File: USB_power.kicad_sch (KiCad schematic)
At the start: 21 parts, among them J1 JST-4-pin, J1 TYPE-C-31-M12_13, U1 BQ24074RGTR, U4 TPD4E05U06DQAR

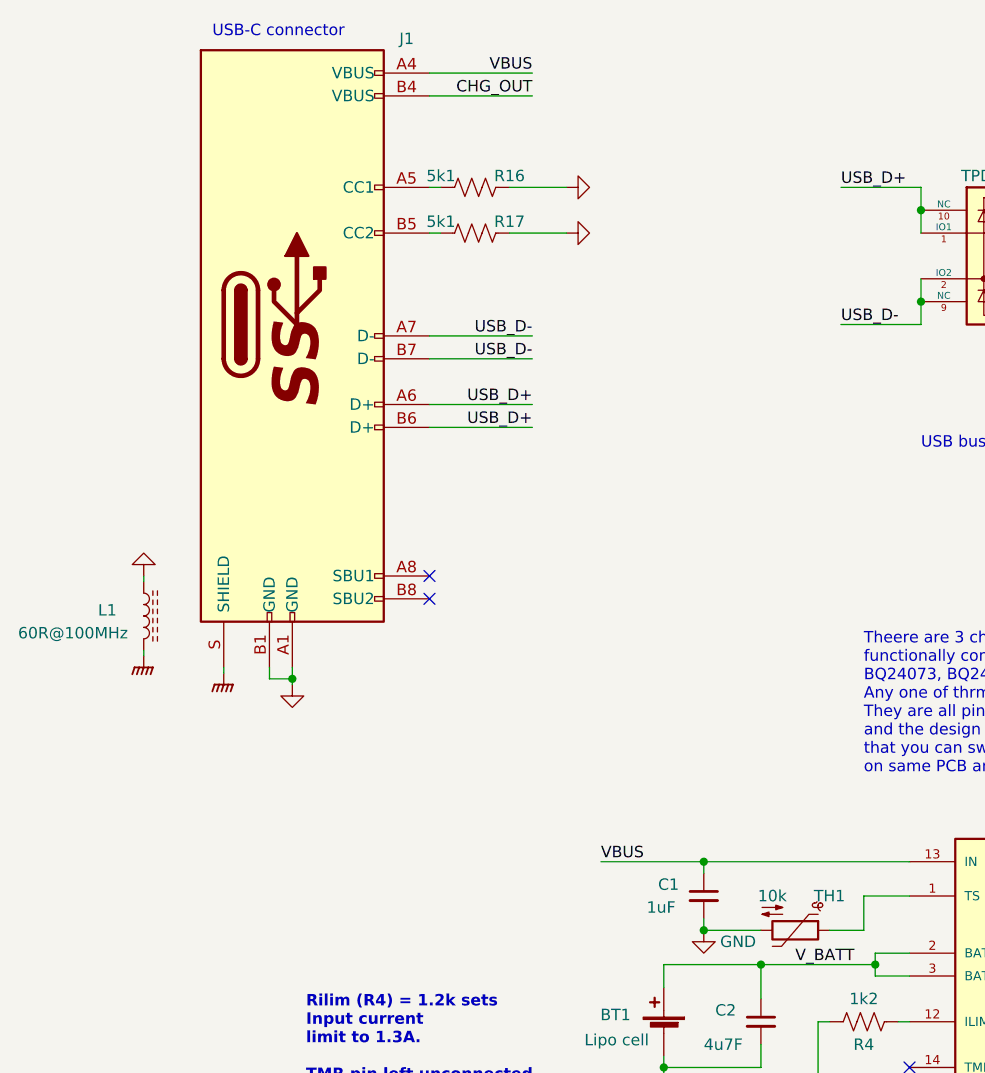
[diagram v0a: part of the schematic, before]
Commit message: RGB and Keys added to sch
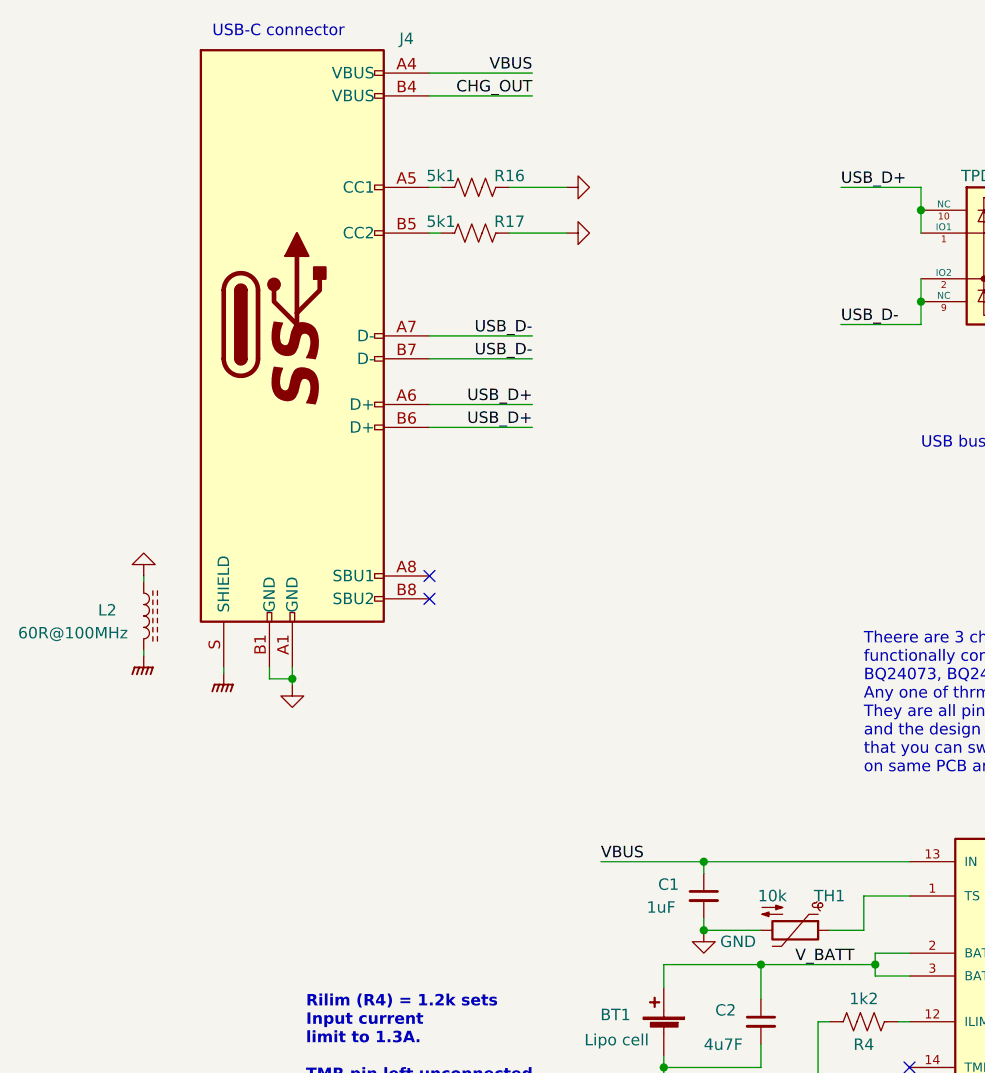
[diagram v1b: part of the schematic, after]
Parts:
- renumbered J1 to J4, L1 to L2

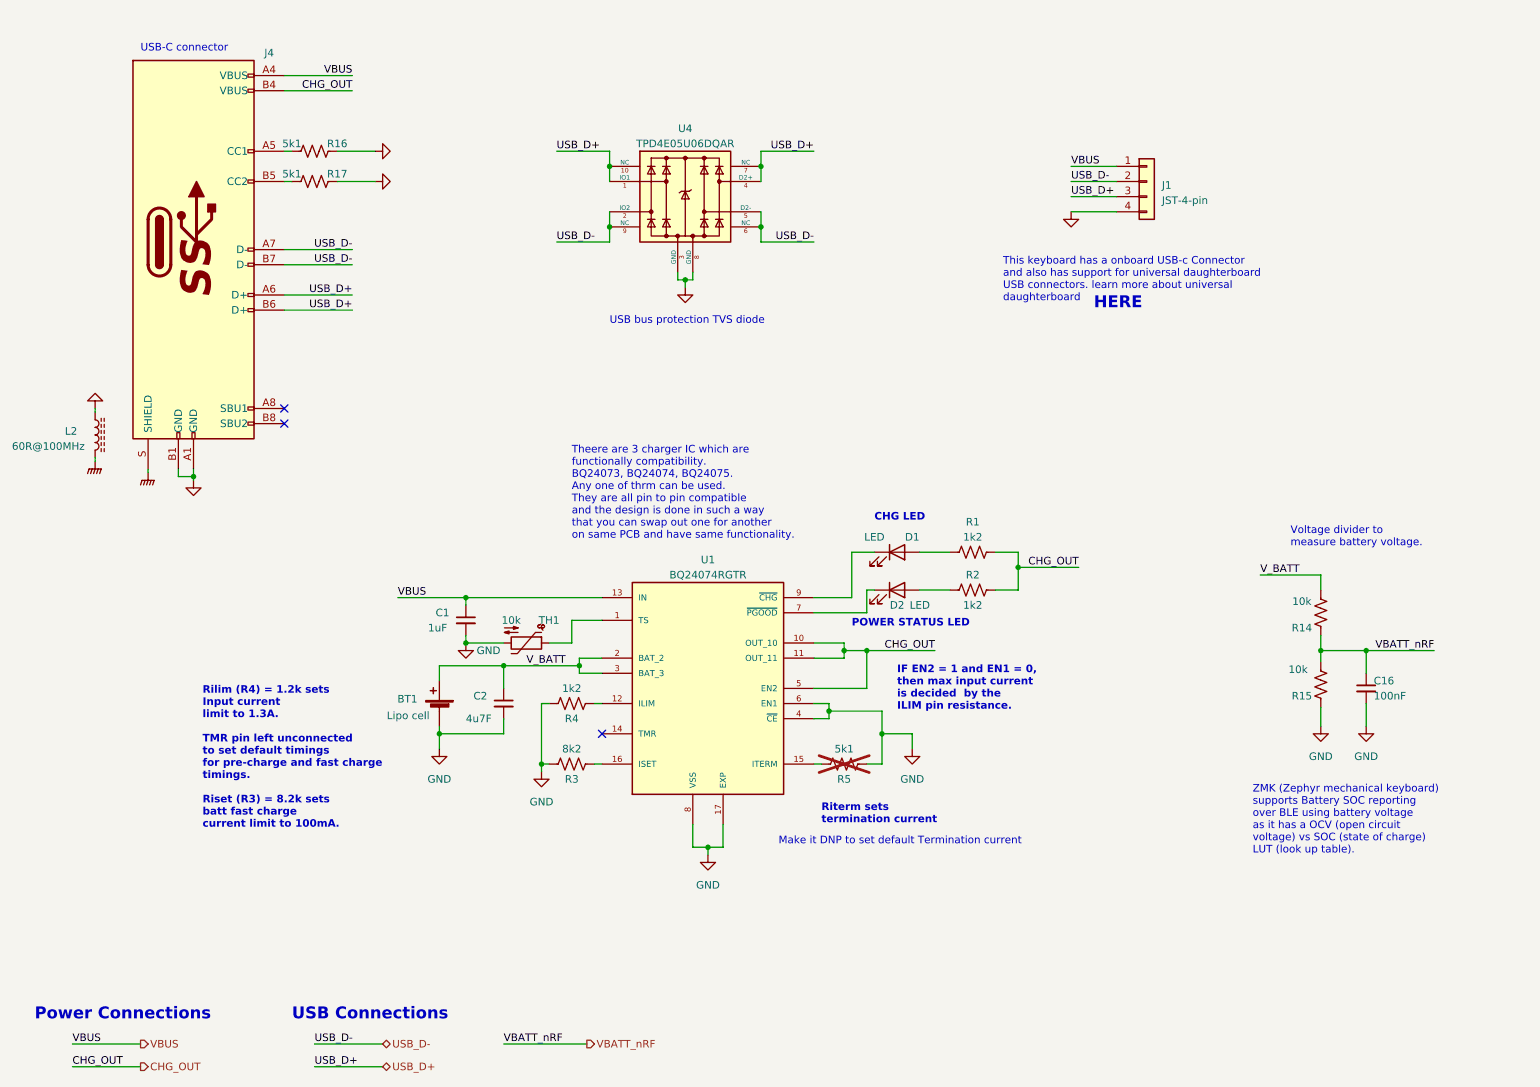
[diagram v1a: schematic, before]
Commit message: Layout start. Add symbols to proj lib
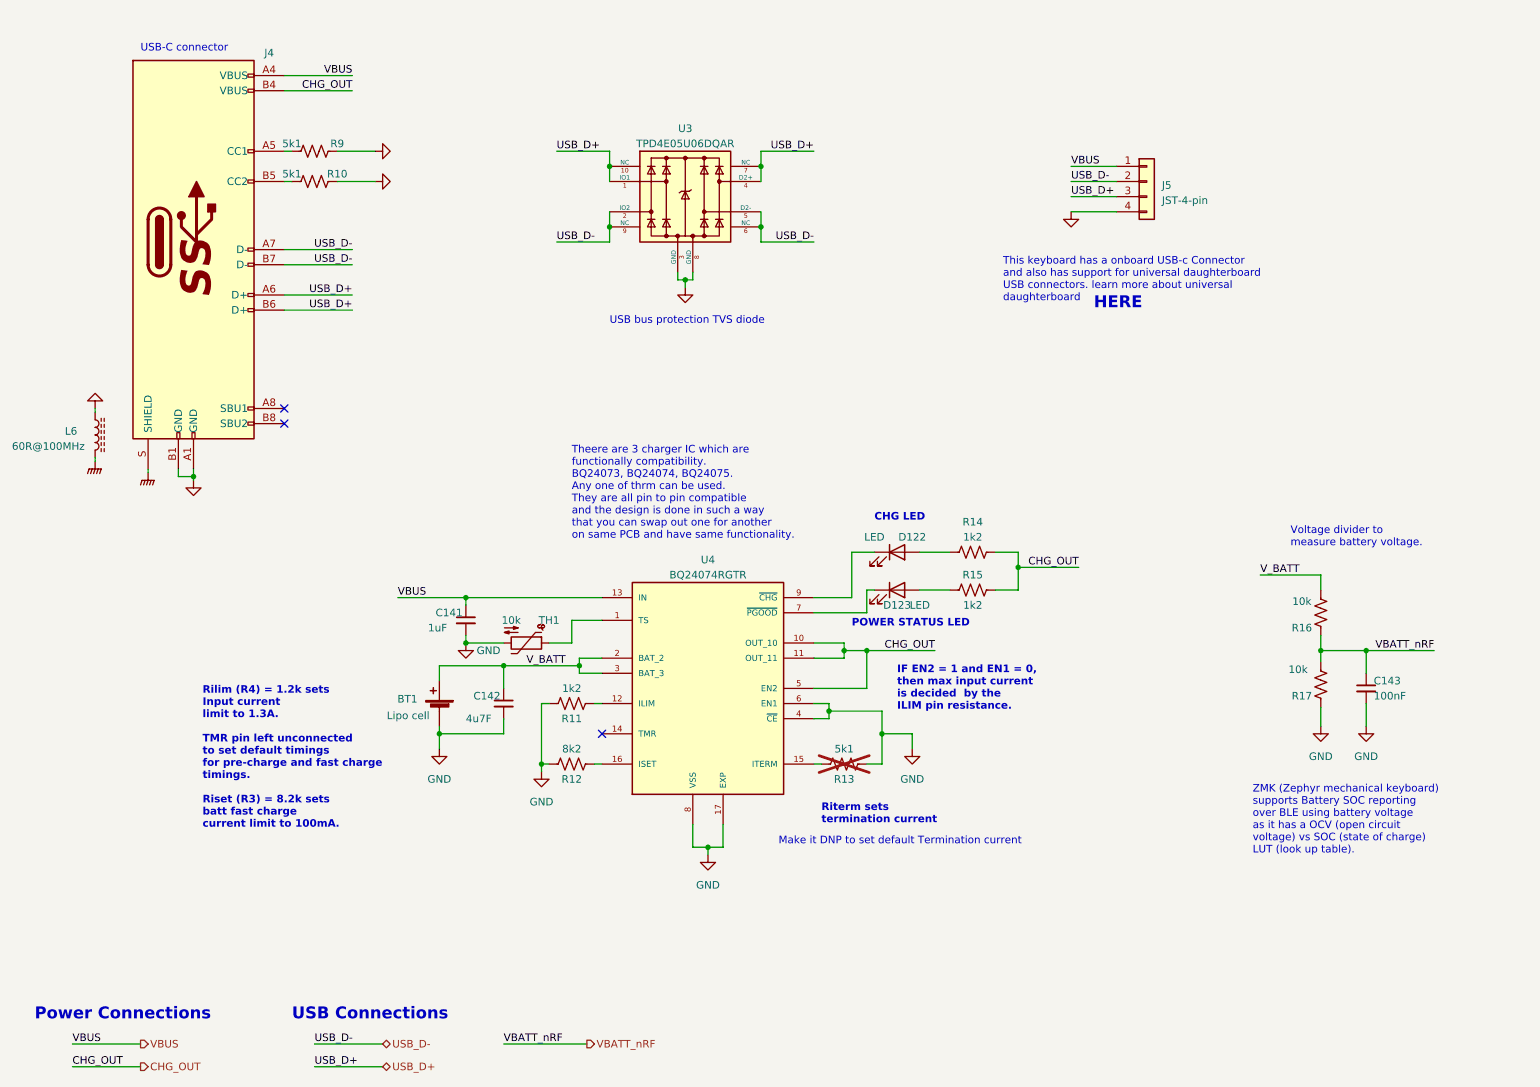
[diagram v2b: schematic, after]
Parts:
- renumbered C1 to C141, C2 to C142, C16 to C143, D1 to D122, D2 to D123, J1 to J5, L2 to L6, R17 to R10, R4 to R11, R3 to R12, R5 to R13, R1 to R14, R2 to R15, R14 to R16, R15 to R17, R16 to R9, U4 to U3, U1 to U4

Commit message: Status LEDs
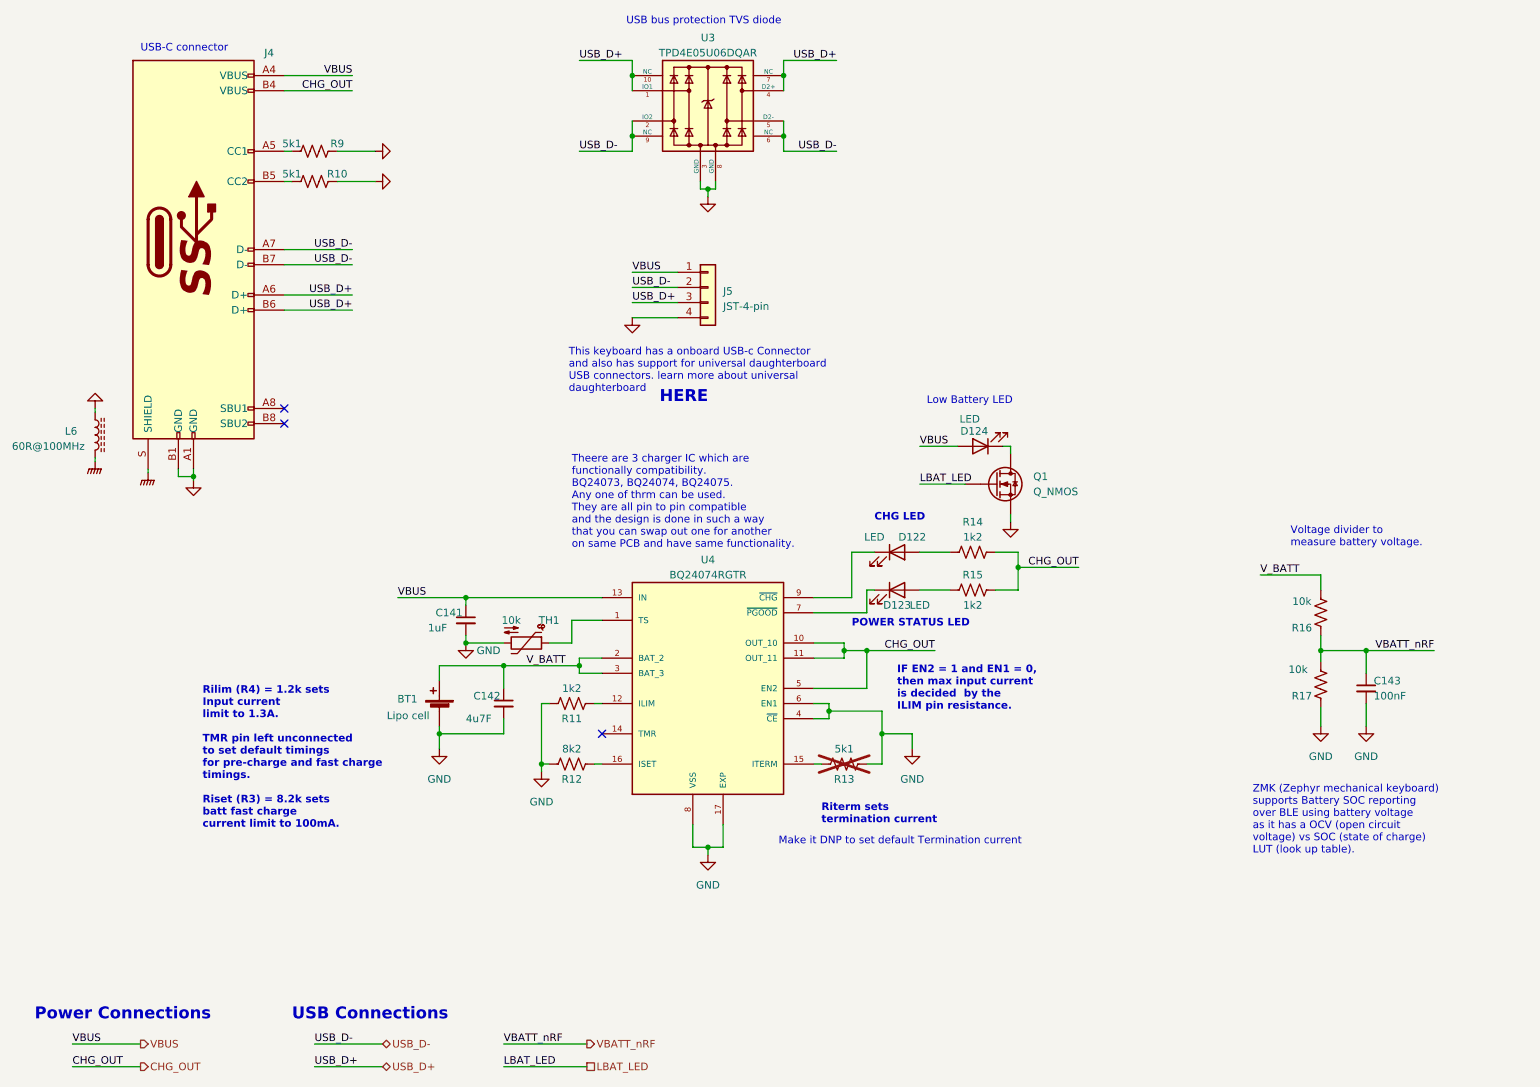
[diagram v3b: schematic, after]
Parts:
- added D124: LED, keyboard:LED_0603_1608Metric, symbol Device:LED
- added Q1: Q_NMOS, keyboard:SOT-23-3, symbol Device:Q_NMOS
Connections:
- net GND: now also Q1.S
- net VBUS: now also D124.2 (A)
- new net: D124.1 (K), Q1.D
- new net LBAT_LED: Q1.G
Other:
- note added: "Low Battery LED"
- moved on the sheet: J5, U3

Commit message: Status LED work
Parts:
- removed D123: LED, keyboard:LED_0603_1608Metric, symbol keyboard:LED
- added R19, R21: R_US, keyboard:R_0402_1005Metric, symbol keyboard:R_US
- R14, R15: value 1k2 -> R_US
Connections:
- net CHG_OUT: no longer R15.1
- net GND: now also R15.2
- net LBAT_LED: now also R21.1; no longer Q1.G
- net VBUS: now also R19.2; no longer D124.2 (A)
- new net: Q1.G, R15.1, R21.2
- new net: D124.2 (A), R19.1
- no-connect marks 3 -> 4
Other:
- note removed: "POWER STATUS LED"
- moved on the sheet: BT1, D122, D124, Q1

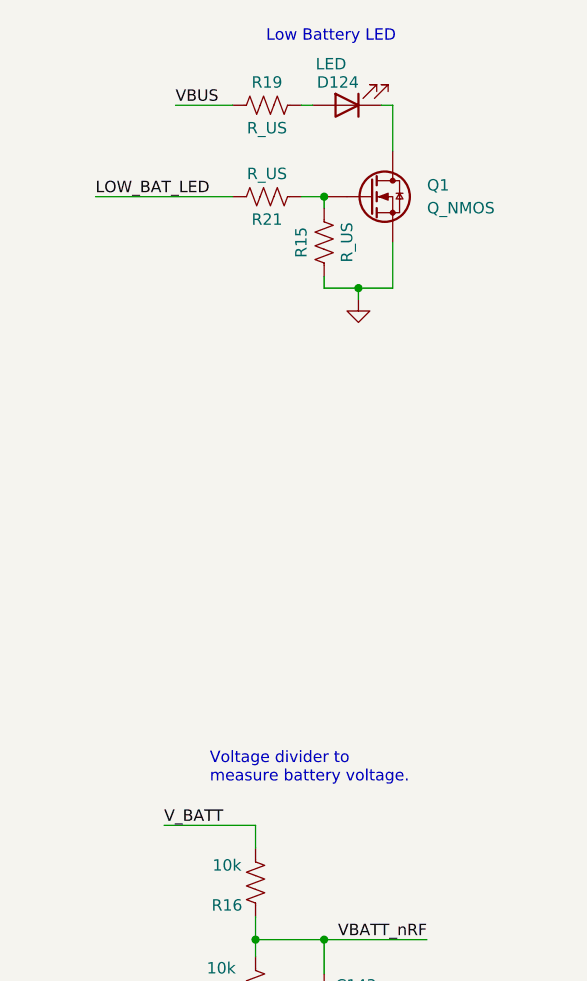
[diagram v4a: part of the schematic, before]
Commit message: Minor sch changes. Work towards matching g915 pcb dimensions
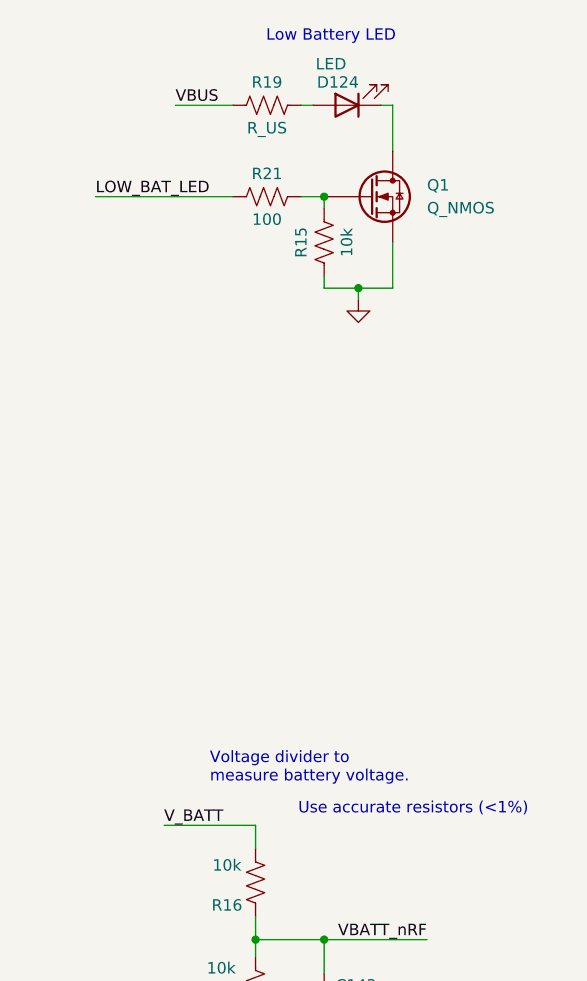
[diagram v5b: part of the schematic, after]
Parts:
- R15: value R_US -> 10k
- R21: value R_US -> 100
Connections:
- net LBAT_LED: now also R21.2; no longer R21.1
- net at Q1.G, R15.1: now also R21.1; no longer R21.2
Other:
- note added: "Use accurate resistors (<1%)"
- moved on the sheet: R21
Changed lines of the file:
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@@
 		(company "HW-tinkerers")
+	)
+	(text "Use accurate resistors (<1%)"
+		(exclude_from_sim no)
+		(at 256.286 106.172 0)
+		(effects
+			(font
+				(size 1.27 1.27)
+			)
+		)
 	)
 	(text "Voltage divider to \nmeasure battery voltage.\n\n"
@@
 			)
 		)
-		(property "Value" "R_US"
+		(property "Value" "10k"
 			(at 248.92 43.18 0)
 			(effects
@@
 	(symbol
 		(lib_id "keyboard:R_US")
-		(at 240.03 38.1 180)
+		(at 240.03 38.1 0)
 		(unit 1)
 		(exclude_from_sim no)
@@
 		(dnp no)
 		(property "Reference" "R21"
+			(at 240.03 35.56 0)
+			(effects
+				(font
+					(size 1.27 1.27)
+				)
+			)
+		)
+		(property "Value" "100"
 			(at 240.03 40.64 0)
 			(effects
@@
 			)
 		)
-		(property "Value" "R_US"
-			(at 240.03 35.56 0)
-			(effects
-				(font
-					(size 1.27 1.27)
-				)
-			)
-		)
 		(property "Footprint" "keyboard:R_0402_1005Metric"
-			(at 240.284 37.084 0)
-			(effects
-				(font
+			(at 239.776 39.116 0)
+			(effects
+				(font
